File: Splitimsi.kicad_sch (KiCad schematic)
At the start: 42 parts, among them SW1 MX_RGB, SW10 MX_RGB, SW11 MX_RGB, SW12 MX_RGB, SW13 MX_RGB, SW14 MX_RGB, SW15 MX_RGB, SW16 MX_RGB, SW17 MX_RGB, SW18 MX_RGB, SW19 MX_RGB, SW2 MX_RGB, SW20 MX_RGB, SW21 MX_RGB, SW22 MX_RGB, SW23 MX_RGB, SW24 MX_RGB, SW25 MX_RGB, SW26 MX_RGB, SW27 MX_RGB, SW28 MX_RGB, SW29 MX_RGB, SW3 MX_RGB, SW4 MX_RGB, SW5 MX_RGB, SW6 RotaryEncoder_Switch, SW7 MX_RGB, SW8 MX_RGB, SW9 MX_RGB, U1 ProMicro, U2 TRRS

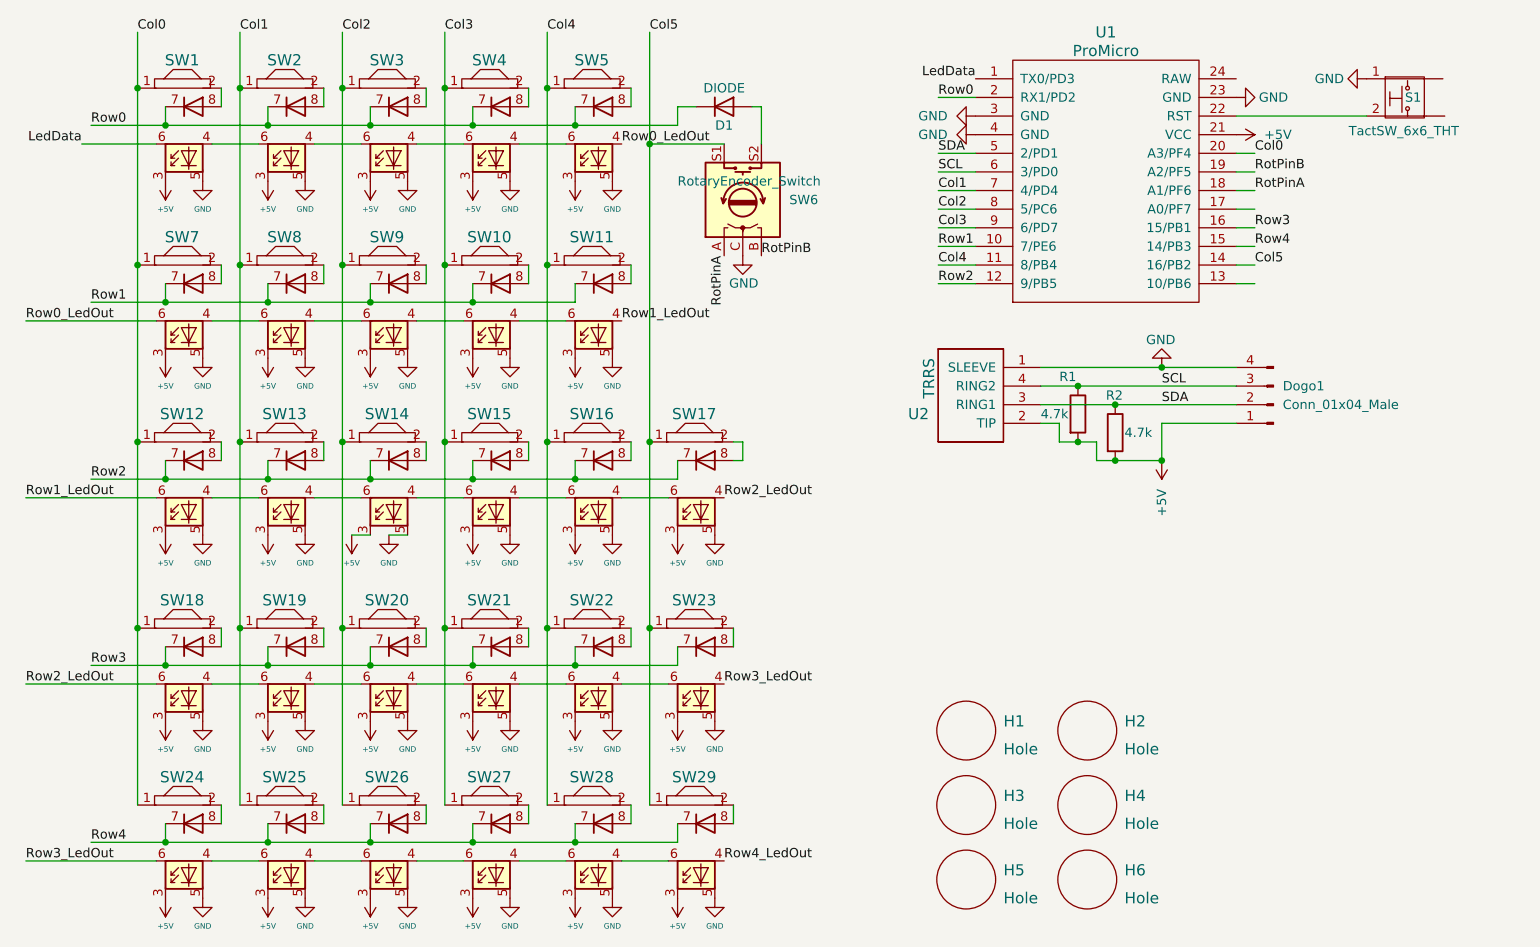
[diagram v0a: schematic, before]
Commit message: 1 extra knob added to the layout
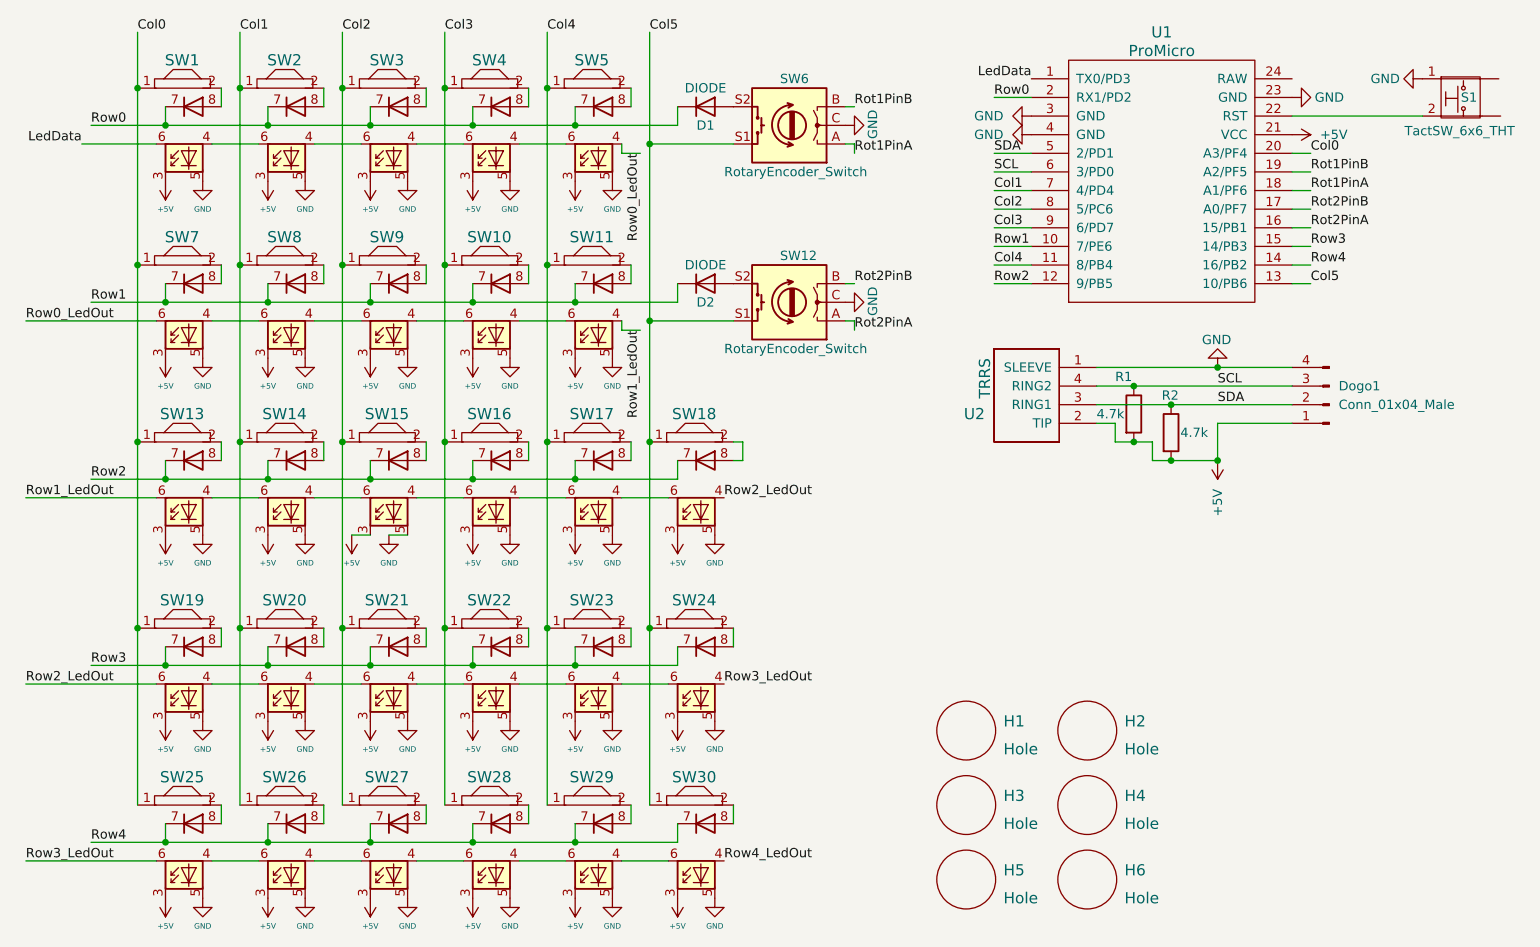
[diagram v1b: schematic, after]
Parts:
- added D2: DIODE, Keebio-Parts:D_SOD123, symbol Simulation_SPICE:DIODE
- added SW12: RotaryEncoder_Switch, Keebio-Parts:RotaryEncoder_EC11, symbol Device:RotaryEncoder_Switch
- renumbered SW12 to SW13, SW13 to SW14, SW14 to SW15, SW15 to SW16, SW16 to SW17, SW17 to SW18, SW18 to SW19, SW19 to SW20, SW20 to SW21, SW21 to SW22, SW22 to SW23, SW23 to SW24, SW24 to SW25, SW25 to SW26, SW26 to SW27, SW27 to SW28, SW28 to SW29, SW29 to SW30
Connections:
- net Col5: now also U1.13 (10/PB6), SW12.S1; no longer U1.14 (16/PB2)
- net GND: now also SW12.C
- net Row1: now also D2.2 (K)
- net Row3: now also U1.15 (14/PB3); no longer U1.16 (15/PB1)
- net Row4: now also U1.14 (16/PB2); no longer U1.15 (14/PB3)
- net Rot2PinB: now reaches U1.17 (A0/PF7)
- net Rot2PinB: now also SW12.B
- net RotPinA renamed Rot1PinA
- net RotPinB renamed Rot1PinB
- new net: D2.1 (A), SW12.S2
- new net Rot2PinA: SW12.A, U1.16 (15/PB1)
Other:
- moved on the sheet: D1, Dogo1, R1, R2, S1, SW6, U1, U2

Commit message: TRRS footprınt changed to surface mount
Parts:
- U2: value TRRS -> (none); footprint Keebio-Parts:TRRS-PJ-320A -> (none)
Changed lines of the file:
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@@
       (effects (font (size 1.524 1.524)) (justify left))
     )
-    (property "Value" "TRRS" (id 1) (at 147.32 59.69 90)
+    (property "Value" "" (id 1) (at 147.32 59.69 90)
       (effects (font (size 1.524 1.524)) (justify left))
     )
-    (property "Footprint" "Keebio-Parts:TRRS-PJ-320A" (id 2) (at 149.86 58.42 0)
+    (property "Footprint" "" (id 2) (at 149.86 58.42 0)
       (effects (font (size 1.524 1.524)) hide)
     )
@@
     )
     (path "/a62bed7d-868a-43a1-b284-68a3824f2abe"
-      (reference "U2") (unit 1) (value "TRRS") (footprint "Keebio-Parts:TRRS-PJ-320A")
-    )
-  )
+      (reference "U2") (unit 1) (value "TRRS") (footprint "Keebio-Parts:TRRS-PJ-320D")
+    )
+  )

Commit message: layout update
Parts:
- SW18: value MX_RGB -> (none); footprint KeyboardCustomFPs:Kailh_HS_MX_LED -> (none)
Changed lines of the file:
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@@
       (effects (font (size 1.524 1.524)))
     )
-    (property "Value" "MX_RGB" (id 1) (at 107.7276 67.3151 0)
-      (effects (font (size 1.524 1.524)) hide)
-    )
-    (property "Footprint" "KeyboardCustomFPs:Kailh_HS_MX_LED" (id 2) (at 106.5571 64.655 0)
+    (property "Value" "" (id 1) (at 107.7276 67.3151 0)
+      (effects (font (size 1.524 1.524)) hide)
+    )
+    (property "Footprint" "" (id 2) (at 106.5571 64.655 0)
       (effects (font (size 1.524 1.524)) hide)
     )
@@
     )
     (path "/26d58434-7bc0-4330-aacc-ebafc1af4dff"
-      (reference "SW18") (unit 1) (value "MX_RGB") (footprint "KeyboardCustomFPs:Kailh_HS_MX_LED")
+      (reference "SW18") (unit 1) (value "MX_RGB") (footprint "KeyboardCustomFPs:Kailh_HS_MX_LED_option2")
     )
     (path "/0cb1d01e-f5f0-4c79-8ca3-b02247355dc9"
@@
     )
     (path "/a62bed7d-868a-43a1-b284-68a3824f2abe"
-      (reference "U2") (unit 1) (value "TRRS") (footprint "Keebio-Parts:TRRS-PJ-320D")
-    )
-  )
+      (reference "U2") (unit 1) (value "TRRS") (footprint "Keebio-Parts:TRRS-PJ-320A")
+    )
+  )

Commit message: Temp reset button added
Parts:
- S1: value TactSW_6x6_THT -> (none); footprint aio3-misc:PushButton_6x6mm_TH_Pretty -> (none)
- SW18: value (none) -> MX_RGB; footprint (none) -> KeyboardCustomFPs:Kailh_HS_MX_LED_option2
- U2: value (none) -> TRRS; footprint (none) -> Keebio-Parts:TRRS-PJ-320A
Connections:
- no-connect marks 0 -> 3
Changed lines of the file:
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@@
   (junction (at 35.56 52.07) (diameter 0) (color 0 0 0 0)
   )
+  (no_connect (at 189.23 21.59))
+  (no_connect (at 217.424 21.59))
+  (no_connect (at 217.678 26.67))
   (wire (pts (xy 71.12 96.52) (xy 71.12 99.06))
     (stroke (width 0) (type default) (color 0 0 0 0))
@@
       (effects (font (size 1.524 1.524)))
     )
-    (property "Value" "" (id 1) (at 107.7276 67.3151 0)
-      (effects (font (size 1.524 1.524)) hide)
-    )
-    (property "Footprint" "" (id 2) (at 106.5571 64.655 0)
+    (property "Value" "MX_RGB" (id 1) (at 107.7276 67.3151 0)
+      (effects (font (size 1.524 1.524)) hide)
+    )
+    (property "Footprint" "KeyboardCustomFPs:Kailh_HS_MX_LED_option2" (id 2) (at 106.5571 64.655 0)
       (effects (font (size 1.524 1.524)) hide)
     )
@@
     (in_bom yes) (on_board yes)
     (property "Reference" "S1" (id 0) (at 213.36 24.13 0))
-    (property "Value" "TactSW_6x6_THT" (id 1) (at 212.09 28.702 0))
-    (property "Footprint" "aio3-misc:PushButton_6x6mm_TH_Pretty" (id 2) (at 212.09 20.066 0)
+    (property "Value" "" (id 1) (at 212.09 28.702 0))
+    (property "Footprint" "" (id 2) (at 212.09 20.066 0)
       (effects (font (size 1.27 1.27)) hide)
     )
@@
       (effects (font (size 1.524 1.524)) (justify left))
     )
-    (property "Value" "" (id 1) (at 147.32 59.69 90)
+    (property "Value" "TRRS" (id 1) (at 147.32 59.69 90)
       (effects (font (size 1.524 1.524)) (justify left))
     )
-    (property "Footprint" "" (id 2) (at 149.86 58.42 0)
+    (property "Footprint" "Keebio-Parts:TRRS-PJ-320A" (id 2) (at 149.86 58.42 0)
       (effects (font (size 1.524 1.524)) hide)
     )
@@
     )
     (path "/a2474201-d835-4ea6-9d62-0592a109ce48"
-      (reference "S1") (unit 1) (value "TactSW_6x6_THT") (footprint "aio3-misc:PushButton_6x6mm_TH_Pretty")
+      (reference "S1") (unit 1) (value "TactSW_6x6_THT") (footprint "Button_Switch_THT:SW_Tactile_SPST_Angled_PTS645Vx58-2LFS")
     )
     (path "/200aa83c-0260-4790-a345-ddeba1e13353"

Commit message: Some ERC errors cleared
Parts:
- R1, R2: value 4.7k -> (none); footprint Resistor_SMD:R_1206_3216Metric_Pad1.30x1.75mm_HandSolder -> (none)
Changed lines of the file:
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@@
     (effects (font (size 1.27 1.27)) (justify left bottom))
   )
-  (label "Row0_LedOut" (at 16.51 54.61 0)
+  (label "Row0_LedOut" (at 16.6584 54.61 0)
     (effects (font (size 1.27 1.27)) (justify left bottom))
   )
@@
     (in_bom yes) (on_board yes)
     (property "Reference" "R1" (id 0) (at 165.1 62.23 0)
+      (effects (font (size 1.27 1.27)) (justify left) hide)
+    )
+    (property "Value" "" (id 1) (at 162.56 67.31 0)
       (effects (font (size 1.27 1.27)) (justify left))
     )
-    (property "Value" "4.7k" (id 1) (at 162.56 67.31 0)
-      (effects (font (size 1.27 1.27)) (justify left))
-    )
-    (property "Footprint" "Resistor_SMD:R_1206_3216Metric_Pad1.30x1.75mm_HandSolder" (id 2) (at 165.862 67.31 90)
+    (property "Footprint" "" (id 2) (at 165.862 67.31 90)
       (effects (font (size 1.27 1.27)) hide)
     )
@@
     (in_bom yes) (on_board yes)
     (property "Reference" "R2" (id 0) (at 171.45 64.77 0)
+      (effects (font (size 1.27 1.27)) (justify left) hide)
+    )
+    (property "Value" "" (id 1) (at 173.99 69.85 0)
       (effects (font (size 1.27 1.27)) (justify left))
     )
-    (property "Value" "4.7k" (id 1) (at 173.99 69.85 0)
-      (effects (font (size 1.27 1.27)) (justify left))
-    )
-    (property "Footprint" "Resistor_SMD:R_1206_3216Metric_Pad1.30x1.75mm_HandSolder" (id 2) (at 170.942 69.85 90)
+    (property "Footprint" "" (id 2) (at 170.942 69.85 90)
       (effects (font (size 1.27 1.27)) hide)
     )
@@
     )
     (path "/a2474201-d835-4ea6-9d62-0592a109ce48"
-      (reference "S1") (unit 1) (value "TactSW_6x6_THT") (footprint "Button_Switch_THT:SW_Tactile_SPST_Angled_PTS645Vx58-2LFS")
+      (reference "S1") (unit 1) (value "TactSW_6x6_THT") (footprint "Button_Switch_THT:SW_Tactile_SPST_Angled_PTS645Vx31-2LFS")
     )
     (path "/200aa83c-0260-4790-a345-ddeba1e13353"

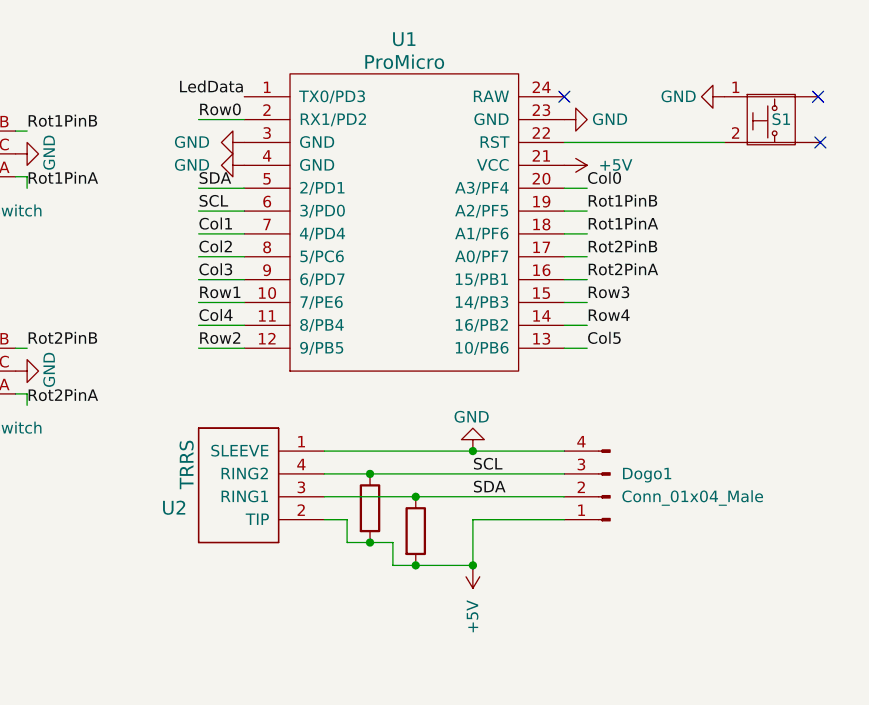
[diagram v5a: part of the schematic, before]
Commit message: Reset footprint changed
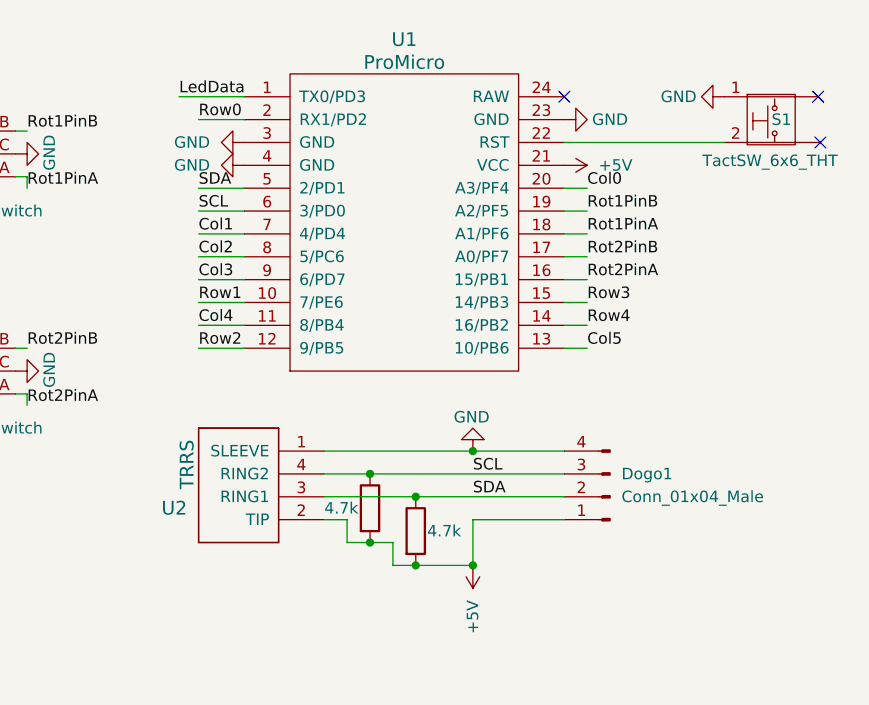
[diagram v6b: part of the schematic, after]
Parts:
- R1, R2: value (none) -> 4.7k; footprint (none) -> Resistor_SMD:R_1206_3216Metric_Pad1.30x1.75mm_HandSolder
- S1: value (none) -> TactSW_6x6_THT; footprint (none) -> aio3-misc:PushButton_6x6mm_TH_Pretty
- SW18: footprint KeyboardCustomFPs:Kailh_HS_MX_LED_option2 -> KeyboardCustomFPs:Kailh_HS_MX_LED

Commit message: reset button 3d view test
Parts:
- S1: value TactSW_6x6_THT -> (none); footprint aio3-misc:PushButton_6x6mm_TH_Pretty -> (none)
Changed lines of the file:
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@@
     (in_bom yes) (on_board yes)
     (property "Reference" "S1" (id 0) (at 213.36 24.13 0))
-    (property "Value" "TactSW_6x6_THT" (id 1) (at 212.09 28.702 0))
-    (property "Footprint" "aio3-misc:PushButton_6x6mm_TH_Pretty" (id 2) (at 212.09 20.066 0)
+    (property "Value" "" (id 1) (at 212.09 28.702 0))
+    (property "Footprint" "" (id 2) (at 212.09 20.066 0)
       (effects (font (size 1.27 1.27)) hide)
     )
@@
     )
     (path "/a2474201-d835-4ea6-9d62-0592a109ce48"
-      (reference "S1") (unit 1) (value "TactSW_6x6_THT") (footprint "aio3-misc:PushButton_6x6mm_TH_Pretty")
+      (reference "S1") (unit 1) (value "TactSW_6x6_THT") (footprint "Button_Switch_SMD:SW_SPST_B3U-1000P")
     )
     (path "/200aa83c-0260-4790-a345-ddeba1e13353"

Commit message: Update Splitimsi.kicad_sch
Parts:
- S1: value (none) -> TactSW_6x6_THT; footprint (none) -> Button_Switch_SMD:SW_SPST_B3U-1000P
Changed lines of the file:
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@@
     (in_bom yes) (on_board yes)
     (property "Reference" "S1" (id 0) (at 213.36 24.13 0))
-    (property "Value" "" (id 1) (at 212.09 28.702 0))
-    (property "Footprint" "" (id 2) (at 212.09 20.066 0)
+    (property "Value" "TactSW_6x6_THT" (id 1) (at 212.09 28.702 0))
+    (property "Footprint" "Button_Switch_SMD:SW_SPST_B3U-1000P" (id 2) (at 212.09 20.066 0)
       (effects (font (size 1.27 1.27)) hide)
     )
